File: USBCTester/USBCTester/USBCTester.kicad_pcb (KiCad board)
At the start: 4 copper layers, 100 x 82.6 mm, 93 parts, among them J1 USB4080-03-A, J2 USB4080-03-A, J3 Conn_01x14, J4 Conn_01x03, J6 Conn_01x03, SW1 SW_Push, U1 74HC595, U2 74HC595, U3 74HC595, U4 74HC595, U5 74HC595, U6 74HC595, U7 RaspberryPi_Pico

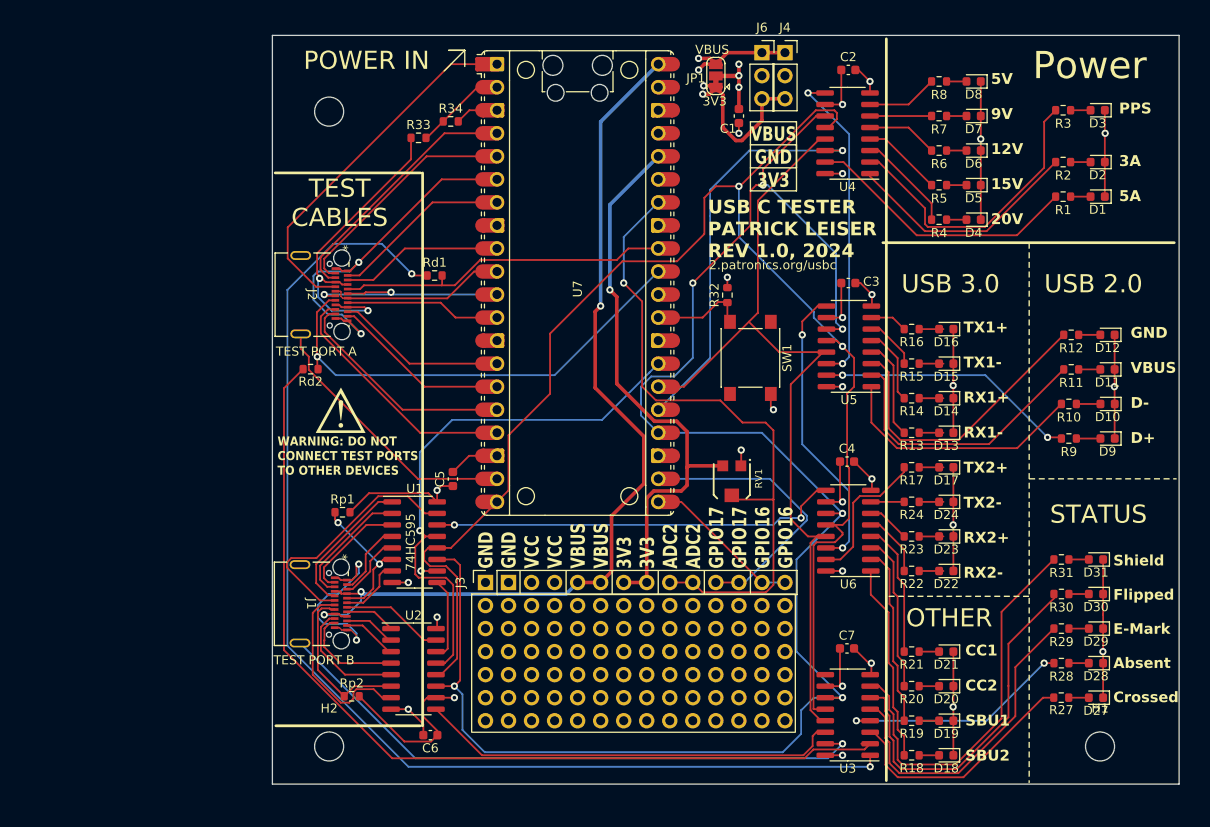
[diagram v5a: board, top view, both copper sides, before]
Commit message: adjust layout to preseve i2c pins, and general layout cleanup
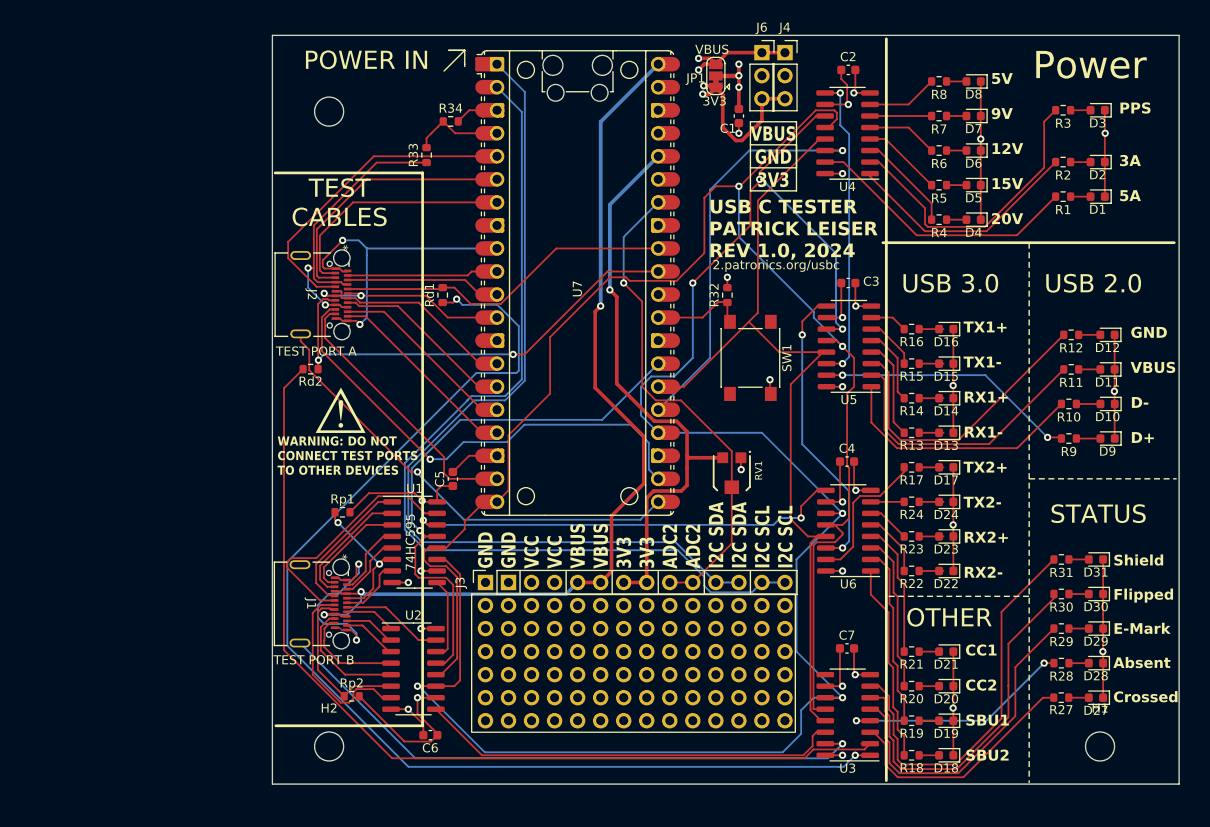
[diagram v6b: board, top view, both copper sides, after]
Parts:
- moved Rd1 2.33 mm to (137.5, 90.2), turned to 90 degrees
- moved R33 2.10 mm to (135.7, 74.8), turned to 90 degrees
- moved RV1 0.89 mm to (169.4, 109.8)
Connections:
- J2 pad 27: Net-(U7-GPIO14) -> Net-(U7-GPIO16)
- J2 pad 28: Net-(U7-GPIO14) -> Net-(U7-GPIO16)
- J2 pad A1: Net-(U7-GPIO4) -> Net-(U7-GPIO6)
- J2 pad A12: Net-(U7-GPIO4) -> Net-(U7-GPIO6)
- J2 pad B1: Net-(U7-GPIO4) -> Net-(U7-GPIO6)
- J2 pad B12: Net-(U7-GPIO4) -> Net-(U7-GPIO6)
- J3 pad 11: GPIO17 -> i2cSDA
- J3 pad 12: GPIO17 -> i2cSDA
- J3 pad 13: GPIO16 -> i2cSCL
- J3 pad 14: GPIO16 -> i2cSCL
- R33 pad 2: Net-(U7-GPIO1) -> Net-(U7-GPIO2)
- R34 pad 1: Net-(U7-GPIO1) -> Net-(U7-GPIO2)
- U7 pad 1: Net-(J2-SBU2) -> i2cSDA
- U7 pad 10: Net-(J2-DN1) -> Net-(J2-SSTXP1)
- U7 pad 11: Net-(J2-DP1) -> Net-(J2-SSTXN1)
- U7 pad 12: Net-(J2-SBU1) -> Net-(J2-DP1)
- U7 pad 14: Net-(J2-SSRXN2) -> Net-(J2-DN1)
- U7 pad 15: Net-(J2-SSRXP2) -> Net-(J2-SBU1)
- U7 pad 16: Net-(J2-SSTXP2) -> Net-(J2-SSRXN2)
- U7 pad 17: Net-(J2-SSTXN2) -> Net-(J2-SSRXP2)
- U7 pad 19: Net-(U7-GPIO14) -> Net-(J2-SSTXP2)
- U7 pad 2: Net-(U7-GPIO1) -> i2cSCL
- U7 pad 21: GPIO16 -> Net-(U7-GPIO16)
- U7 pad 22: GPIO17 -> Net-(J2-SSTXN2)
- U7 pad 4: Net-(J2-SSRXN1) -> Net-(U7-GPIO2)
- U7 pad 5: Net-(J2-SSRXP1) -> Net-(J2-SBU2)
- U7 pad 6: Net-(U7-GPIO4) -> Net-(J2-SSRXN1)
- U7 pad 7: Net-(J2-SSTXP1) -> Net-(J2-SSRXP1)
- U7 pad 9: Net-(J2-SSTXN1) -> Net-(U7-GPIO6)
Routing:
- net i2cSCL: track 0.00 -> 105.4 mm
- net i2cSDA: track 0.00 -> 99.3 mm
- net Net-(U7-GPIO16): track 0.00 -> 50.7 mm, vias 0 -> 1
- net Net-(U7-GPIO4): track 40.7 -> 0.00 mm, vias 2 -> 0
- net Net-(U7-GPIO6): track 0.00 -> 36.5 mm, vias 0 -> 2
- net GPIO17: track 31.4 -> 0.00 mm
- net Net-(U7-GPIO14): track 29.6 -> 0.00 mm
- net Net-(J2-SSTXN2): track 27.8 -> 53.0 mm, vias 0 -> 1
- net GPIO28: track 73.0 -> 54.4 mm
- net GPIO16: track 17.7 -> 0.00 mm
- net Net-(U7-GPIO1): track 10.1 -> 0.00 mm
- net Net-(U7-GPIO2): track 0.00 -> 10.1 mm
- net Net-(J2-SBU2): track 40.5 -> 35.2 mm
- net Net-(J2-SSTXP2): track 25.4 -> 29.9 mm
- net GND: track 145.5 -> 149.0 mm
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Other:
- board text added: "GND GND VCC VCC VBUS VBUS 3V3 3V3 ADC2 ADC2 I2C SDA I2C SDA I2C SCL I2C SCL"
- board text removed: "GND GND VCC VCC VBUS VBUS 3V3 3V3 ADC2 ADC2 GPIO17 GPIO17 GPIO16 GPIO16"

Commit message: minor cleanup and reorganization
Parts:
- added C8: C, Capacitor_SMD:C_0603_1608Metric, F.Cu at (178.7, 65.4)
- added C9: C, Capacitor_SMD:C_0603_1608Metric, F.Cu at (178.7, 63.3)
- moved C2 1.40 mm to (183.6, 65.4)
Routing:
- net Net-(U3-~{OE}): track 94.4 -> 101.5 mm
- net GND: track 149.0 -> 156.0 mm
- net Net-(U7-GPIO6): track 36.5 -> 30.0 mm
- net VBUS: track 115.0 -> 117.6 mm
- net +3V3: track 83.0 -> 85.5 mm
- net RCLK: track 169.8 -> 171.3 mm
- net Net-(U3-QB): track 128.5 -> 129.0 mm
- added copper zone on F.Cu, net (none)

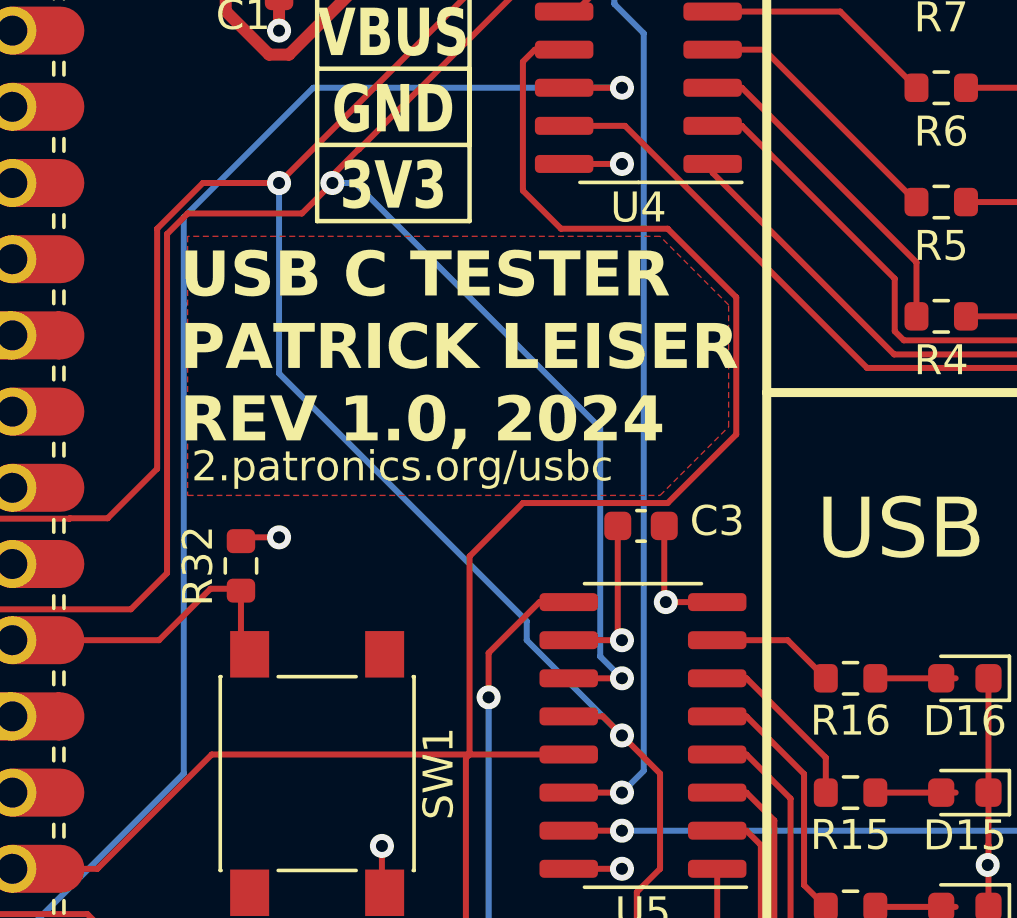
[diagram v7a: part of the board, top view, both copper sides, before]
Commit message: adjust text background style, last 7.0 commit
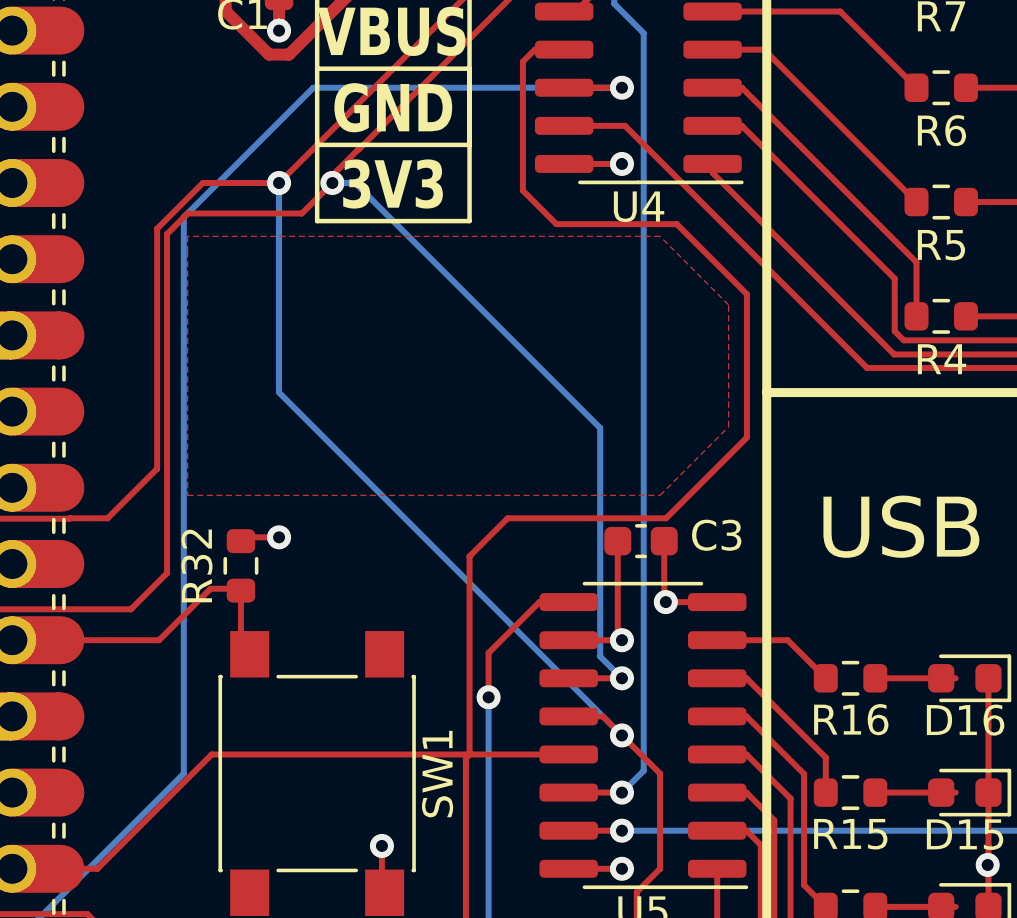
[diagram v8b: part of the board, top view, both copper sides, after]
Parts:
- moved C3 0.51 mm to (182.2, 89.4)
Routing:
- net Net-(U3-~{OE}): track 101.5 -> 102.3 mm
- net VCC: track 77.7 -> 77.2 mm
- net GND: track 156.0 -> 155.5 mm
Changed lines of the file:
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@@
   )
   (footprint "Capacitor_SMD:C_0603_1608Metric" (layer "F.Cu")
-    (at 182.245 88.9)
+    (at 182.245 89.408)
     (descr "Capacitor SMD 0603 (1608 Metric), square (rectangular) end terminal, IPC_7351 nominal, (Body size source: IPC-SM-782 page 76, https://www.pcb-3d.com/wordpress/wp-content/uploads/ipc-sm-782a_amendment_1_and_2.pdf), generated with kicad-footprint-generator")
     (tags "capacitor")
@@
   (gr_rect (start 118.745 61.595) (end 218.7194 144.145)
     (stroke (width 0.1) (type default)) (fill none) (layer "Edge.Cuts"))
+  (gr_text "USB C TESTER\nPATRICK LEISER\nREV 1.0, 2024" (at 166.878 86.233) (layer "F.Paste")
+    (effects (font (size 1.5 1.5) (thickness 0.3) bold) (justify left bottom))
+  )
+  (gr_text "2.patronics.org/usbc" (at 167.259 87.503) (layer "F.Paste")
+    (effects (font (size 1 1) (thickness 0.15)) (justify left bottom))
+  )
   (gr_text "GND\nGND\nVCC\nVCC\nVBUS\nVBUS\n3V3\n3V3\nADC2\nADC2\nI2C SDA\nI2C SDA\nI2C SCL\nI2C SCL" (at 176.276 120.269 90) (layer "B.SilkS")
     (effects (font (size 1.58 1.2) (thickness 0.2) bold) (justify right bottom mirror))
@@
     (effects (font (size 1 1) (thickness 0.15)) (justify left bottom))
   )
-  (gr_text "USB C TESTER\nPATRICK LEISER\nREV 1.0, 2024" (at 166.878 86.233) (layer "F.SilkS")
-    (effects (font (size 1.5 1.5) (thickness 0.3) bold) (justify left bottom))
-  )
-  (gr_text "2.patronics.org/usbc" (at 167.259 87.503) (layer "F.SilkS")
-    (effects (font (size 1 1) (thickness 0.15)) (justify left bottom))
-  )
   (gr_text "STATUS" (at 204.47 115.57) (layer "F.SilkS")
     (effects (font (size 2 2) (thickness 0.2)) (justify left bottom))
@@
   (segment (start 193.8275 115.5955) (end 193.8275 120.65) (width 0.2) (layer "F.Cu") (net 17))
   (segment (start 140.462 69.85) (end 143.51 69.85) (width 0.2) (layer "F.Cu") (net 17))
-  (segment (start 183.02 88.9) (end 183.02 91.388) (width 0.2) (layer "F.Cu") (net 17))
   (segment (start 183.02 67.7795) (end 182.8545 67.945) (width 0.2) (layer "F.Cu") (net 17))
   (segment (start 179.445 63.336) (end 178.61 64.171) (width 0.4) (layer "F.Cu") (net 17))
-  (segment (start 183.02 91.388) (end 183.072 91.44) (width 0.2) (layer "F.Cu") (net 17))
   (segment (start 133.731 135.89) (end 131.826 135.89) (width 0.2) (layer "F.Cu") (net 17))
   (segment (start 128.27 119.888) (end 128.016 120.142) (width 0.2) (layer "F.Cu") (net 17))
@@
   (segment (start 193.8275 109.22) (end 193.8275 115.5445) (width 0.2) (layer "F.Cu") (net 17))
   (segment (start 126.2775 121.65076) (end 126.01988 121.39314) (width 0.2) (layer "F.Cu") (net 17))
+  (segment (start 183.02 91.388) (end 183.072 91.44) (width 0.2) (layer "F.Cu") (net 17))
   (segment (start 193.8275 99.5425) (end 193.802 99.568) (width 0.2) (layer "F.Cu") (net 17))
   (segment (start 170.18 89.281) (end 169.037 89.281) (width 0.2) (layer "F.Cu") (net 17))
   (segment (start 210.3375 130.81) (end 210.3375 134.62) (width 0.2) (layer "F.Cu") (net 17))
   (segment (start 170.399 108.167) (end 170.399 109.439) (width 0.2) (layer "F.Cu") (net 17))
+  (segment (start 183.02 89.408) (end 183.02 91.388) (width 0.2) (layer "F.Cu") (net 17))
   (segment (start 135.388 137.547) (end 133.731 135.89) (width 0.2) (layer "F.Cu") (net 17))
   (segment (start 128.016 127.762) (end 128.016 128.27) (width 0.13) (layer "F.Cu") (net 17))
@@
   (via (at 181.61 95.885) (size 0.8) (drill 0.4) (layers "F.Cu" "B.Cu") (net 81))
   (via (at 170.18 77.47) (size 0.8) (drill 0.4) (layers "F.Cu" "B.Cu") (net 81))
-  (segment (start 170.18 83.82) (end 170.18 77.47) (width 0.2) (layer "B.Cu") (net 81))
-  (segment (start 178.435 92.71) (end 178.435 92.075) (width 0.2) (layer "B.Cu") (net 81))
-  (segment (start 181.61 95.885) (end 178.435 92.71) (width 0.2) (layer "B.Cu") (net 81))
-  (segment (start 178.435 92.075) (end 170.18 83.82) (width 0.2) (layer "B.Cu") (net 81))
+  (segment (start 170.18 84.455) (end 170.18 77.47) (width 0.2) (layer "B.Cu") (net 81))
+  (segment (start 181.61 95.885) (end 170.18 84.455) (width 0.2) (layer "B.Cu") (net 81))
   (segment (start 135.636 116.84) (end 134.498 117.978) (width 0.2) (layer "F.Cu") (net 82))
   (segment (start 134.498 121.014) (end 134.874 121.39) (width 0.2) (layer "F.Cu") (net 82))
@@
   (segment (start 179.301592 69.215) (end 179.6825 69.215) (width 0.2) (layer "F.Cu") (net 94))
   (segment (start 170.18 66.04) (end 170.18 67.31) (width 0.4) (layer "F.Cu") (net 94))
-  (segment (start 181.47 92.57) (end 181.61 92.71) (width 0.2) (layer "F.Cu") (net 94))
   (segment (start 181.61 140.97) (end 179.705 140.97) (width 0.2) (layer "F.Cu") (net 94))
   (segment (start 170.18 64.77) (end 170.18 66.04) (width 0.4) (layer "F.Cu") (net 94))
   (segment (start 136.938 138.751) (end 136.938 138.589) (width 0.2) (layer "F.Cu") (net 94))
   (segment (start 181.61 113.03) (end 179.77 113.03) (width 0.2) (layer "F.Cu") (net 94))
+  (segment (start 181.47 92.57) (end 181.61 92.71) (width 0.2) (layer "F.Cu") (net 94))
   (segment (start 181.61 92.71) (end 179.835 92.71) (width 0.2) (layer "F.Cu") (net 94))
   (segment (start 136.938 138.751) (end 136.233 139.456) (width 0.2) (layer "F.Cu") (net 94))
   (segment (start 170.18 66.04) (end 170.15 66.07) (width 0.2) (layer "F.Cu") (net 94))
+  (segment (start 181.47 89.408) (end 181.47 92.57) (width 0.2) (layer "F.Cu") (net 94))
   (segment (start 181.33 108.585) (end 181.33 112.75) (width 0.2) (layer "F.Cu") (net 94))
   (segment (start 136.906 113.03) (end 135.382 113.03) (width 0.2) (layer "F.Cu") (net 94))
@@
   (segment (start 134.427001 112.075001) (end 129.395999 112.075001) (width 0.2) (layer "F.Cu") (net 94))
   (segment (start 173.609 99.568) (end 173.609 101.039) (width 0.2) (layer "F.Cu") (net 94))
-  (segment (start 181.47 88.9) (end 181.47 92.57) (width 0.2) (layer "F.Cu") (net 94))
   (segment (start 182.118 66.154) (end 182.118 69.088) (width 0.2) (layer "F.Cu") (net 94))
   (segment (start 135.255 112.903) (end 134.427001 112.075001) (width 0.2) (layer "F.Cu") (net 94))
@@
   (segment (start 124.474 96.76) (end 123.825 97.409) (width 0.2) (layer "B.Cu") (net 105))
   (segment (start 145.274 96.76) (end 124.474 96.76) (width 0.2) (layer "B.Cu") (net 105))
+  (segment (start 179.6825 73.025) (end 178.707501 73.025) (width 0.2) (layer "F.Cu") (net 106))
   (segment (start 178.308 73.424501) (end 178.308 77.724) (width 0.2) (layer "F.Cu") (net 106))
   (segment (start 178.054 116.84) (end 179.77 116.84) (width 0.2) (layer "F.Cu") (net 106))
   (segment (start 176.408 115.448) (end 176.784 115.824) (width 0.2) (layer "F.Cu") (net 106))
-  (segment (start 185.42 81.28) (end 185.42 85.852) (width 0.2) (layer "F.Cu") (net 106))
+  (segment (start 185.7756 81.1784) (end 185.7756 85.9536) (width 0.2) (layer "F.Cu") (net 106))
+  (segment (start 176.53 89.916) (end 176.53 96.52) (width 0.2) (layer "F.Cu") (net 106))
   (segment (start 167.935 96.52) (end 176.53 96.52) (width 0.2) (layer "F.Cu") (net 106))
   (segment (start 179.23831 137.16) (end 179.705 137.16) (width 0.2) (layer "F.Cu") (net 106))
-  (segment (start 183.134 78.994) (end 185.42 81.28) (width 0.2) (layer "F.Cu") (net 106))
+  (segment (start 179.4256 78.8416) (end 183.4388 78.8416) (width 0.2) (layer "F.Cu") (net 106))
   (segment (start 178.075001 117.56) (end 178.075001 135.996691) (width 0.2) (layer "F.Cu") (net 106))
-  (segment (start 178.308 88.138) (end 176.53 89.916) (width 0.2) (layer "F.Cu") (net 106))
+  (segment (start 178.308 77.724) (end 179.4256 78.8416) (width 0.2) (layer "F.Cu") (net 106))
   (segment (start 178.075001 117.56) (end 178.054 117.538999) (width 0.2) (layer "F.Cu") (net 106))
+  (segment (start 183.0832 88.646) (end 177.8 88.646) (width 0.2) (layer "F.Cu") (net 106))
   (segment (start 179.77 116.84) (end 178.795001 116.84) (width 0.2) (layer "F.Cu") (net 106))
-  (segment (start 176.53 89.916) (end 176.53 96.52) (width 0.2) (layer "F.Cu") (net 106))
+  (segment (start 185.7756 85.9536) (end 183.0832 88.646) (width 0.2) (layer "F.Cu") (net 106))
   (segment (start 178.707501 73.025) (end 178.308 73.424501) (width 0.2) (layer "F.Cu") (net 106))
-  (segment (start 183.134 88.138) (end 178.308 88.138) (width 0.2) (layer "F.Cu") (net 106))
   (segment (start 161.29 100.33) (end 164.125 100.33) (width 0.2) (layer "F.Cu") (net 106))
   (segment (start 176.53 96.52) (end 176.408 96.642) (width 0.2) (layer "F.Cu") (net 106))
   (segment (start 176.53 96.52) (end 179.835 96.52) (width 0.2) (layer "F.Cu") (net 106))
-  (segment (start 179.6825 73.025) (end 178.707501 73.025) (width 0.2) (layer "F.Cu") (net 106))
   (segment (start 177.8 116.84) (end 178.054 116.84) (width 0.2) (layer "F.Cu") (net 106))
   (segment (start 178.054 117.538999) (end 178.054 116.84) (width 0.2) (layer "F.Cu") (net 106))
@@
   (segment (start 176.784 115.824) (end 177.8 116.84) (width 0.2) (layer "F.Cu") (net 106))
   (segment (start 178.075001 135.996691) (end 179.23831 137.16) (width 0.2) (layer "F.Cu") (net 106))
-  (segment (start 179.578 78.994) (end 183.134 78.994) (width 0.2) (layer "F.Cu") (net 106))
-  (segment (start 178.308 77.724) (end 179.578 78.994) (width 0.2) (layer "F.Cu") (net 106))
-  (segment (start 185.42 85.852) (end 183.134 88.138) (width 0.2) (layer "F.Cu") (net 106))
+  (segment (start 183.4388 78.8416) (end 185.7756 81.1784) (width 0.2) (layer "F.Cu") (net 106))
+  (segment (start 177.8 88.646) (end 176.53 89.916) (width 0.2) (layer "F.Cu") (net 106))
   (segment (start 121.86742 95.32442) (end 121.86742 94.50578) (width 0.2) (layer "F.Cu") (net 107))
   (segment (start 122.809 96.266) (end 121.86742 95.32442) (width 0.2) (layer "F.Cu") (net 107))
